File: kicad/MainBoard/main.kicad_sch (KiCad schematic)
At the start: 81 parts, among them J1 TRG1, J10 I2C, J2 TRG2, J3 Conn_02x04_Odd_Even, J4 AudioJack3_SwitchTR, J5 Conn_02x04_Odd_Even, J6 LCD, J7 ACC Port, J8 FrontPanel, J9 433TX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

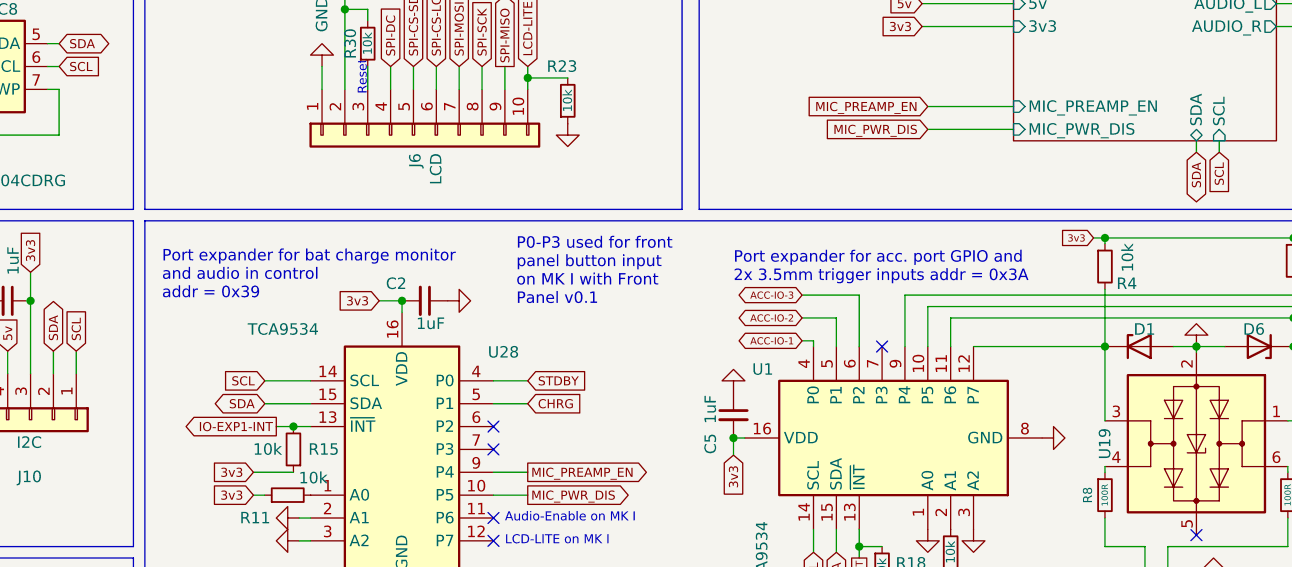
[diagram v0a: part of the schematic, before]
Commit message: fix i2c address for port expanders on schematic
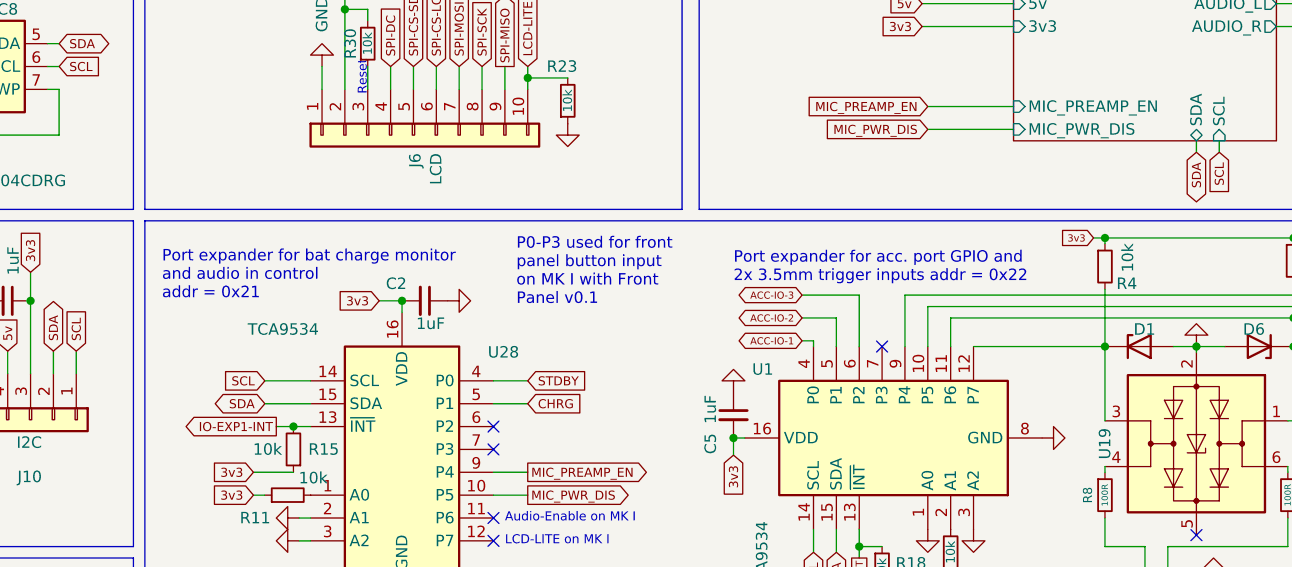
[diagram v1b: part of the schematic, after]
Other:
- note added: "Port expander for acc. port GPIO and 2x 3.5mm trigger inputs addr = 0x22"
- note added: "Port expander for bat charge monitor and audio in control addr = 0x21"
- note removed: "Port expander for acc. port GPIO and 2x 3.5mm trigger inputs addr = 0x3A"
- note removed: "Port expander for bat charge monitor and audio in control addr = 0x39"
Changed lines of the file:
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@@
     (effects (font (size 1 1)) (justify left bottom))
   )
-  (text "Port expander for acc. port GPIO and \n2x 3.5mm trigger inputs addr = 0x3A"
+  (text "Port expander for acc. port GPIO and \n2x 3.5mm trigger inputs addr = 0x22"
     (at 187.325 119.38 0)
     (effects (font (size 1.27 1.27)) (justify left bottom))
@@
     (effects (font (size 1.27 1.27)) (justify left bottom))
   )
-  (text "Port expander for bat charge monitor\nand audio in control\naddr = 0x39"
+  (text "Port expander for bat charge monitor\nand audio in control\naddr = 0x21"
     (at 123.825 121.285 0)
     (effects (font (size 1.27 1.27)) (justify left bottom))

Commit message: Add PCB v2.3 kicad project files + gerbers
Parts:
- removed R12, R13: 100k, Resistor_SMD:R_0603_1608Metric_Pad0.98x0.95mm_HandSolder, symbol Device:R_Small
- removed R30: 10k, Resistor_SMD:R_0603_1608Metric_Pad0.98x0.95mm_HandSolder, symbol Device:R_Small
- C1: value 100nF -> 1uF; LCSC C14663 -> C15849
- J6: footprint Connector_PinSocket_2.54mm:PinSocket_1x10_P2.54mm_Vertical -> Connector_Molex:Molex_KK-254_AE-6410-10A_1x10_P2.54mm_Vertical
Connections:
- net 5v: now also J6.9 (Pin_9); no longer J6.2 (Pin_2)
- net GND: now also J6.10 (Pin_10); no longer J6.1 (Pin_1)
- net LCD-LITE: now also J6.1 (Pin_1); no longer J6.10 (Pin_10)
- net SPI-CS-LCD: now also J6.5 (Pin_5); no longer J6.6 (Pin_6)
- net SPI-CS-SD: now also J6.6 (Pin_6); no longer J6.5 (Pin_5)
- net SPI-DC: now also J6.7 (Pin_7); no longer J6.4 (Pin_4)
- net SPI-MISO: now also J6.2 (Pin_2); no longer J6.9 (Pin_9)
- net SPI-MOSI: now also J6.4 (Pin_4); no longer J6.7 (Pin_7)
- net SPI-SCK: now also J6.3 (Pin_3); no longer J6.8 (Pin_8)
- net USB-SENSE: now reaches U3.31 (GPIO26_ADC0)
- net LCD-RESET: now reaches U28.12 (P7)
- net LCD-RESET: now also J6.8 (Pin_8)
- net USB_SENSE1: now reaches U28.6 (P2)
- net USB_SENSE2: now reaches U28.7 (P3)
- net 4v renamed 3.5v
- no-connect marks 27 -> 24
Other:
- sheet Audio ports: added none; removed 3v3
- sheet Output ports: added 3.5v; removed 4v
- sheet Power ports: added 3.5v, 3v3, SW_SENSE1, SW_SENSE2, USB-SENSE; removed 4v, USB-VBUS
- note removed: "Reset"
- moved on the sheet: J6

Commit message: Mainboard PCB v2.4
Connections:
- net PWR_EN: now reaches U3.37 (3V3_EN)
- no-connect marks 24 -> 23
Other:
- sheet Power ports: added PWR_EN; removed none
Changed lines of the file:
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@@
   (title_block
     (title "ZC95 MKII")
-    (rev "2.3")
+    (rev "2.4")
     (company "CrashOverride85")
   )
@@
   (no_connect (at 160.655 145.415))
   (no_connect (at 243.205 152.4))
-  (no_connect (at 160.02 25.4))
   (no_connect (at 238.76 147.32))
   (no_connect (at 24.765 131.445))
@@
     (stroke (width 0) (type default) (color 0 0 0 0))
   )
+  (wire (pts (xy 63.5 35.56) (xy 65.405 35.56))
+    (stroke (width 0) (type default) (color 0 0 0 0))
+  )
   (wire (pts (xy 88.9 55.88) (xy 90.17 55.88))
     (stroke (width 0) (type default) (color 0 0 0 0))
@@
     (stroke (width 0) (type default) (color 0 0 0 0))
   )
+  (wire (pts (xy 160.02 25.4) (xy 161.925 25.4))
+    (stroke (width 0) (type default) (color 0 0 0 0))
+  )
   (wire (pts (xy 121.92 38.1) (xy 124.46 38.1))
     (stroke (width 0) (type default) (color 0 0 0 0))
@@
     )
   )
+  (global_label "PWR_EN" (shape output) (at 65.405 35.56 0) (fields_autoplaced)
+    (effects (font (size 1 1)) (justify left))
+    (property "Intersheet References" "${INTERSHEET_REFS}" (id 0) (at 73.1621 35.4975 0)
+      (effects (font (size 1 1)) (justify left) hide)
+    )
+  )
   (global_label "ACC-IO-1" (shape bidirectional) (at 194.945 125.73 180) (fields_autoplaced)
     (effects (font (size 0.7874 0.7874)) (justify right))
@@
     )
   )
+  (global_label "PWR_EN" (shape input) (at 161.925 25.4 0) (fields_autoplaced)
+    (effects (font (size 1 1)) (justify left))
+    (property "Intersheet References" "${INTERSHEET_REFS}" (id 0) (at 169.6821 25.3375 0)
+      (effects (font (size 1 1)) (justify left) hide)
+    )
+  )
   (global_label "LCD-LITE" (shape input) (at 164.465 95.25 90) (fields_autoplaced)
     (effects (font (size 1 1)) (justify left))
@@
     )
   )
-  (sheet (at 20.955 22.86) (size 42.545 12.7) (fields_autoplaced)
+  (sheet (at 20.955 22.86) (size 42.545 14.605) (fields_autoplaced)
     (stroke (width 0.1524) (type solid) (color 0 0 0 0))
     (fill (color 0 0 0 0.0000))
@@
       (effects (font (size 1.27 1.27)) (justify left bottom))
     )
-    (property "Sheet file" "power.kicad_sch" (id 1) (at 20.955 36.1446 0)
+    (property "Sheet file" "power.kicad_sch" (id 1) (at 20.955 38.0496 0)
       (effects (font (size 1.27 1.27)) (justify left top))
     )
@@
       (effects (font (size 1.27 1.27)) (justify left))
     )
+    (pin "PWR_EN" output (at 63.5 35.56 0)
+      (effects (font (size 1.27 1.27)) (justify right))
+    )
   )
   (sheet (at 90.17 53.975) (size 16.51 16.51)
@@
       (reference "#PWR017") (unit 1) (value "GND") (footprint "")
     )
+    (path "/3f31ae8f-beda-448d-904b-b027dde59383/14a7286b-13dc-4309-b043-a9d9998c9ad1"
+      (reference "#PWR018") (unit 1) (value "GND") (footprint "")
+    )
     (path "/e3bd3ec7-187a-4418-963f-3981fcc1d584"
       (reference "#PWR019") (unit 1) (value "GND") (footprint "")
@@
       (reference "#PWR0139") (unit 1) (value "GND") (footprint "")
     )
+    (path "/3f31ae8f-beda-448d-904b-b027dde59383/da24a002-3f9b-4d73-865c-25c617a92d88"
+      (reference "#PWR0140") (unit 1) (value "GND") (footprint "")
+    )
+    (path "/3f31ae8f-beda-448d-904b-b027dde59383/5ef46222-d4ee-47bb-949b-7756111a2fe7"
+      (reference "#PWR0141") (unit 1) (value "GND") (footprint "")
+    )
     (path "/3f31ae8f-beda-448d-904b-b027dde59383/53f4d707-46cb-43a6-85a4-c81f59e9bc44"
       (reference "BT1") (unit 1) (value "26650 Cell") (footprint "ProjLib:BH-26650-A5BJ001")
@@
       (reference "C62") (unit 1) (value "10nF") (footprint "Capacitor_SMD:C_0603_1608Metric_Pad1.08x0.95mm_HandSolder")
     )
+    (path "/3f31ae8f-beda-448d-904b-b027dde59383/8d140277-ec49-4cbc-9992-d1dc9cf0f903"
+      (reference "C63") (unit 1) (value "DNP") (footprint "Resistor_SMD:R_0805_2012Metric_Pad1.20x1.40mm_HandSolder")
+    )
     (path "/7e1b2806-18f3-4f58-a91f-e94638c09ec3/b3fa6c87-e308-4f3e-99c0-c646354bd9e7"
       (reference "C64") (unit 1) (value "22uF") (footprint "Capacitor_SMD:C_0805_2012Metric_Pad1.18x1.45mm_HandSolder")
@@
       (reference "C70") (unit 1) (value "10uF") (footprint "Capacitor_SMD:C_0603_1608Metric_Pad1.08x0.95mm_HandSolder")
     )
+    (path "/3f31ae8f-beda-448d-904b-b027dde59383/a3d30024-e668-429c-9d2c-2ec079775795"
+      (reference "C71") (unit 1) (value "DNP") (footprint "Capacitor_SMD:C_0603_1608Metric_Pad1.08x0.95mm_HandSolder")
+    )
     (path "/05181b46-a6ce-4485-95c2-87132c085994"
       (reference "D1") (unit 1) (value "BZX584C3V6") (footprint "Diode_SMD:D_SOD-523")
@@
       (reference "R29") (unit 1) (value "100R") (footprint "Resistor_SMD:R_0603_1608Metric_Pad0.98x0.95mm_HandSolder")
     )
+    (path "/3f31ae8f-beda-448d-904b-b027dde59383/476e1c15-d48c-4efc-9488-85c248f31d80"
+      (reference "R30") (unit 1) (value "100R") (footprint "Resistor_SMD:R_0603_1608Metric_Pad0.98x0.95mm_HandSolder")
+    )
     (path "/d3709e09-b881-4dd2-94c0-c5d5e86e2c2a"
       (reference "R31") (unit 1) (value "100R") (footprint "Resistor_SMD:R_0603_1608Metric_Pad0.98x0.95mm_HandSolder")
@@
     )
     (path "/7e1b2806-18f3-4f58-a91f-e94638c09ec3/9fcdc051-0088-4b5c-8cfd-e107d6b0431d"
-      (reference "R36") (unit 1) (value "0.5R") (footprint "Resistor_SMD:R_1218_3246Metric_Pad1.22x4.75mm_HandSolder")
+      (reference "R36") (unit 1) (value "0.5R") (footprint "Resistor_SMD:R_2512_6332Metric_Pad1.40x3.35mm_HandSolder")
     )
     (path "/7e1b2806-18f3-4f58-a91f-e94638c09ec3/9a4b7665-2e91-4b1d-8893-67aacc71bc94"
@@
     )
     (path "/7e1b2806-18f3-4f58-a91f-e94638c09ec3/7d464f86-e1d0-4afa-8f23-6731f0be1e5b"
-      (reference "R61") (unit 1) (value "0.5R") (footprint "Resistor_SMD:R_1218_3246Metric_Pad1.22x4.75mm_HandSolder")
+      (reference "R61") (unit 1) (value "0.5R") (footprint "Resistor_SMD:R_2512_6332Metric_Pad1.40x3.35mm_HandSolder")
     )
     (path "/7e1b2806-18f3-4f58-a91f-e94638c09ec3/424e8034-7b35-4bca-b9fc-cb3b381830e3"
@@
       (reference "R150") (unit 1) (value "100k") (footprint "Resistor_SMD:R_0603_1608Metric_Pad0.98x0.95mm_HandSolder")
     )
+    (path "/3f31ae8f-beda-448d-904b-b027dde59383/6216be2c-c271-4cc0-8930-2df57eafdae7"
+      (reference "R151") (unit 1) (value "10k") (footprint "Resistor_SMD:R_0603_1608Metric_Pad0.98x0.95mm_HandSolder")
+    )
+    (path "/7e1b2806-18f3-4f58-a91f-e94638c09ec3/fe129e04-cb36-40ce-933c-dad354a31229"
+      (reference "R152") (unit 1) (value "10k") (footprint "Resistor_SMD:R_0603_1608Metric_Pad0.98x0.95mm_HandSolder")
+    )
     (path "/3f31ae8f-beda-448d-904b-b027dde59383/9020a93f-838e-47c1-a901-a4b6668a7af9"
       (reference "R153") (unit 1) (value "330K") (footprint "Resistor_SMD:R_0603_1608Metric_Pad0.98x0.95mm_HandSolder")
@@
       (reference "R154") (unit 1) (value "4k7") (footprint "Resistor_SMD:R_0603_1608Metric_Pad0.98x0.95mm_HandSolder")
     )
-    (path "/3f31ae8f-beda-448d-904b-b027dde59383/2e2aa4e4-a5bf-4bc7-a8c5-9a0216055847"
-      (reference "SW1") (unit 1) (value "Power switch") (footprint "ProjLib:SS-12D06L5")
+    (path "/3f31ae8f-beda-448d-904b-b027dde59383/1845e032-fcd8-4154-a5a6-3a8bee70f41c"
+      (reference "SW1") (unit 1) (value "SW_SPDT") (footprint "ProjLib:SS-12D06L5")
     )
     (path "/3f31ae8f-beda-448d-904b-b027dde59383/dbbe00aa-667c-4016-a2d4-1615841e2af5"
